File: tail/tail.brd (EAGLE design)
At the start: 63.2 x 30.5 mm, 6 parts

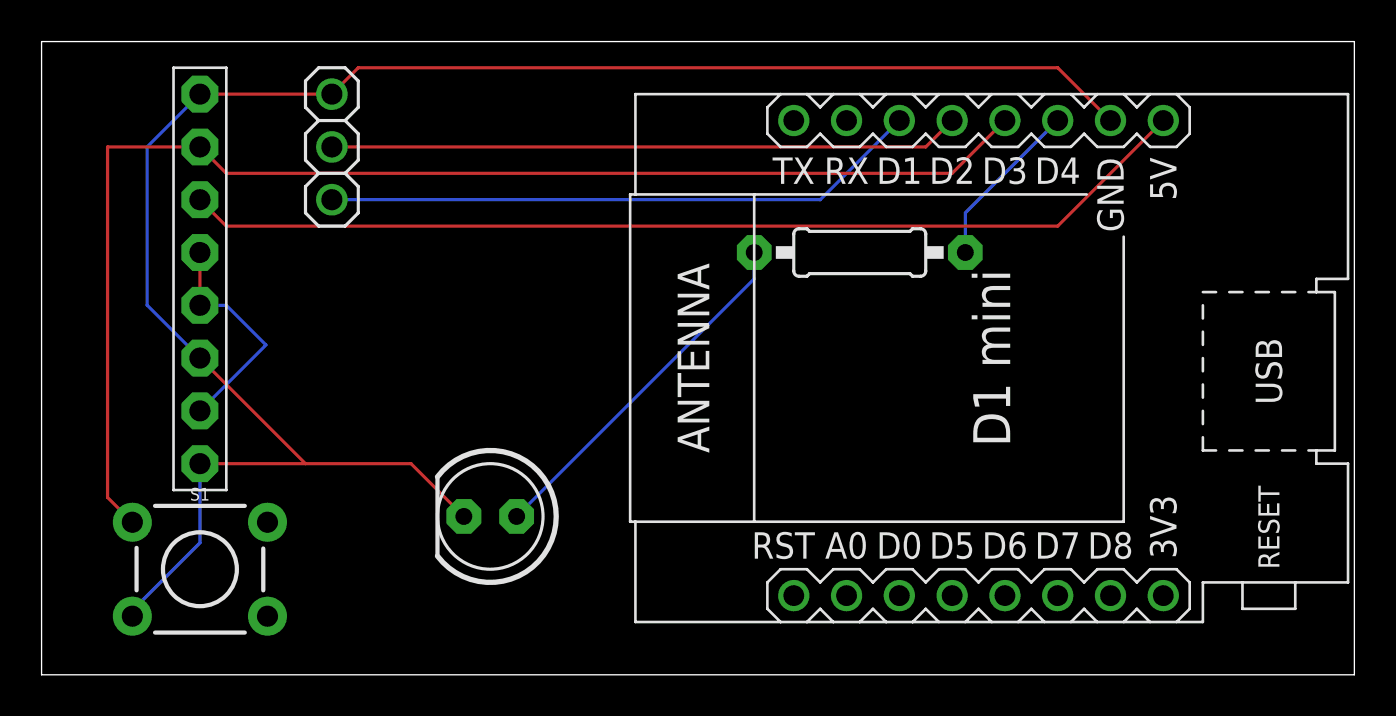
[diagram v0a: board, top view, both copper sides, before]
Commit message: Corrected spelling
On the PC, #include is not case sensitive. It is on Linux.
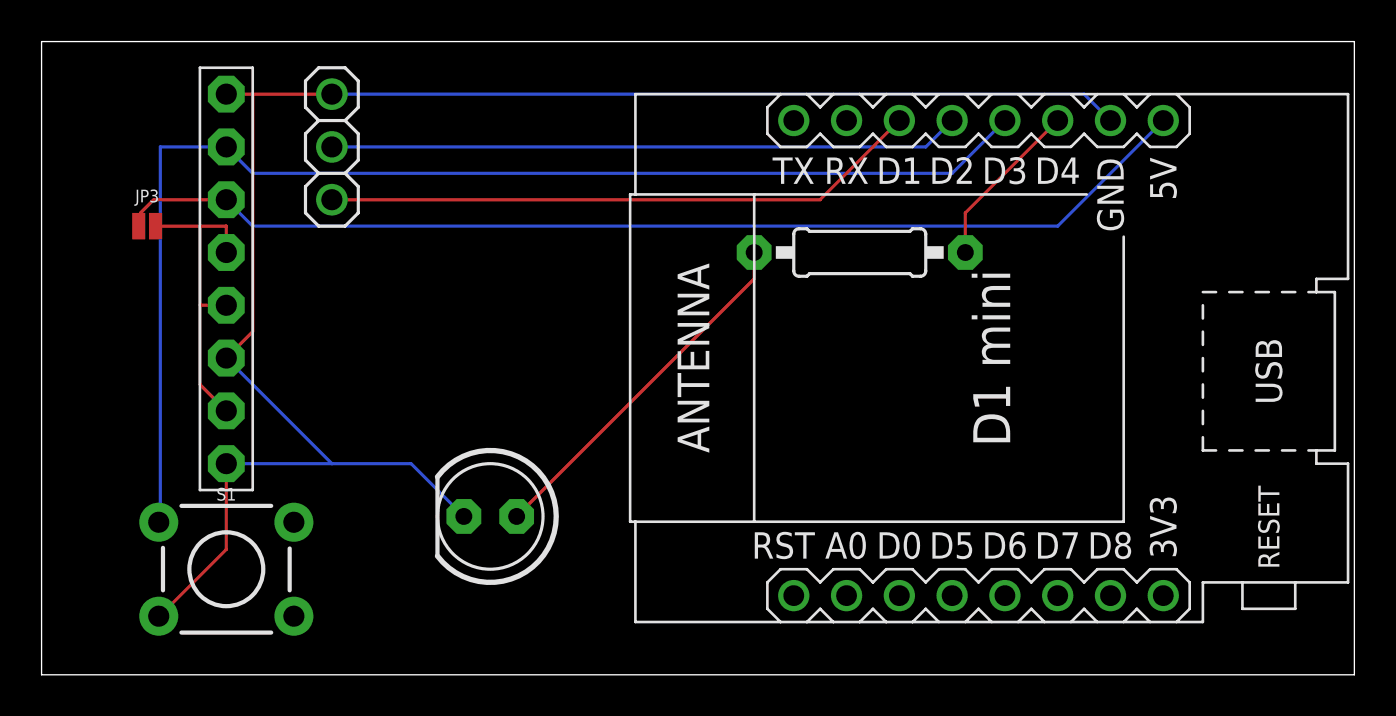
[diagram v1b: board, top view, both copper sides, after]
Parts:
- added JP3: (no value), SparkFun-Jumpers:SMT-JUMPER_2_NC_PASTE_NO-SILK
- moved JP1 1.27 mm to (8.89, 68.6)
- moved S1 1.27 mm to (8.89, 54.6)
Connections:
- net N$4: now also JP3.2
- net N$6: now also JP3.1
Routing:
- net 0: track 89.8 -> 84.7 mm
- net N$4: track 11.0 -> 15.4 mm
- net N$6: track 49.0 -> 52.8 mm
- net N$10: track 63.3 -> 60.3 mm
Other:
- board text added: "H-Bridge"
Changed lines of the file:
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@@
 <text x="2.794" y="77.597" size="1.27" layer="27" rot="R270">G +5  G +5    JMP  BTN</text>
 <text x="15.875" y="77.978" size="1.27" layer="27" rot="R270">D1 D2 G</text>
+<text x="18.415" y="77.978" size="1.27" layer="27" rot="R270">H-Bridge</text>
 </plain>
 <attributes>
@@
 <attribute name="VALUE" x="18.3896" y="58.9534" size="1.27" layer="27" ratio="10" rot="R180"/>
 </element>
-<element name="JP1" library="adafruit" package="1X08-BIG" value="" x="7.62" y="68.58" smashed="yes" rot="R90">
-<attribute name="VALUE" x="10.795" y="58.42" size="1.27" layer="27" rot="R90"/>
+<element name="JP1" library="adafruit" package="1X08-BIG" value="" x="8.89" y="68.58" smashed="yes" rot="R90">
+<attribute name="VALUE" x="12.065" y="58.42" size="1.27" layer="27" rot="R90"/>
 </element>
 <element name="R4" library="adafruit" library_urn="urn:adsk.eagle:library:420" package="0207/10" package3d_urn="urn:adsk.eagle:package:6240597/1" value="1K" x="39.37" y="69.85" smashed="yes">
@@
 <attribute name="VALUE" x="10.795" y="78.74" size="1.27" layer="27" rot="R270"/>
 </element>
-<element name="S1" library="SparkFun-Switches" library_urn="urn:adsk.eagle:library:535" package="TACTILE_SWITCH_PTH_6.0MM" package3d_urn="urn:adsk.eagle:package:40163/1" value="MOMENTARY-SWITCH-SPST-PTH-6.0MM" x="7.62" y="54.61" smashed="yes">
-<attribute name="NAME" x="7.62" y="57.912" size="0.6096" layer="25" font="vector" ratio="20" align="bottom-center"/>
-<attribute name="PROD_ID" value=" SWCH-08441" x="7.62" y="54.61" size="1.778" layer="27" display="off"/>
-<attribute name="SF_SKU" value="COM-00097" x="7.62" y="54.61" size="1.778" layer="27" display="off"/>
-<attribute name="VALUE" x="7.62" y="51.435" size="0.6096" layer="27" font="vector" ratio="20" align="top-center" display="off"/>
+<element name="S1" library="SparkFun-Switches" library_urn="urn:adsk.eagle:library:535" package="TACTILE_SWITCH_PTH_6.0MM" package3d_urn="urn:adsk.eagle:package:40163/1" value="MOMENTARY-SWITCH-SPST-PTH-6.0MM" x="8.89" y="54.61" smashed="yes">
+<attribute name="NAME" x="8.89" y="57.912" size="0.6096" layer="25" font="vector" ratio="20" align="bottom-center"/>
+<attribute name="PROD_ID" value=" SWCH-08441" x="8.89" y="54.61" size="1.778" layer="27" display="off"/>
+<attribute name="SF_SKU" value="COM-00097" x="8.89" y="54.61" size="1.778" layer="27" display="off"/>
+<attribute name="VALUE" x="8.89" y="51.435" size="0.6096" layer="27" font="vector" ratio="20" align="top-center" display="off"/>
+</element>
+<element name="JP3" library="SparkFun-Jumpers" library_urn="urn:adsk.eagle:library:528" package="SMT-JUMPER_2_NC_PASTE_NO-SILK" package3d_urn="urn:adsk.eagle:package:39283/1" value="" x="5.08" y="71.12" smashed="yes">
+<attribute name="NAME" x="5.08" y="72.263" size="0.6096" layer="25" font="vector" ratio="20" align="bottom-center"/>
+<attribute name="VALUE" x="5.08" y="69.977" size="0.6096" layer="27" font="vector" ratio="20" align="top-center"/>
 </element>
 </elements>
@@
 <contactref element="JP1" pad="8"/>
 <contactref element="S1" pad="3"/>
-<wire x1="17.78" y1="59.69" x2="20.32" y2="57.15" width="0.1524" layer="1"/>
-<wire x1="7.62" y1="59.69" x2="12.7" y2="59.69" width="0.1524" layer="1"/>
-<wire x1="12.7" y1="59.69" x2="17.78" y2="59.69" width="0.1524" layer="1"/>
-<wire x1="12.7" y1="59.69" x2="7.62" y2="64.77" width="0.1524" layer="1"/>
-<wire x1="7.62" y1="55.88" x2="4.445" y2="52.705" width="0.1524" layer="16"/>
-<wire x1="7.62" y1="59.69" x2="7.62" y2="55.88" width="0.1524" layer="16"/>
-<wire x1="4.445" y1="52.705" x2="4.3688" y2="52.3494" width="0.1524" layer="16"/>
-<wire x1="48.895" y1="78.74" x2="51.435" y2="76.2" width="0.1524" layer="1"/>
-<wire x1="48.895" y1="78.74" x2="15.24" y2="78.74" width="0.1524" layer="1"/>
-<wire x1="13.97" y1="77.47" x2="15.24" y2="78.74" width="0.1524" layer="1"/>
-<wire x1="13.97" y1="77.47" x2="7.62" y2="77.47" width="0.1524" layer="1"/>
-<wire x1="5.08" y1="67.31" x2="7.62" y2="64.77" width="0.1524" layer="16"/>
-<wire x1="5.08" y1="74.93" x2="5.08" y2="67.31" width="0.1524" layer="16"/>
-<wire x1="7.62" y1="77.47" x2="5.08" y2="74.93" width="0.1524" layer="16"/>
+<wire x1="17.78" y1="59.69" x2="20.32" y2="57.15" width="0.1524" layer="16"/>
+<wire x1="8.89" y1="59.69" x2="13.97" y2="59.69" width="0.1524" layer="16"/>
+<wire x1="13.97" y1="59.69" x2="17.78" y2="59.69" width="0.1524" layer="16"/>
+<wire x1="13.97" y1="59.69" x2="8.89" y2="64.77" width="0.1524" layer="16"/>
+<wire x1="8.89" y1="55.5625" x2="5.715" y2="52.3875" width="0.1524" layer="1"/>
+<wire x1="8.89" y1="59.69" x2="8.89" y2="55.5625" width="0.1524" layer="1"/>
+<wire x1="5.715" y1="52.3875" x2="5.6388" y2="52.3494" width="0.1524" layer="1"/>
+<wire x1="50.165" y1="77.47" x2="51.435" y2="76.2" width="0.1524" layer="16"/>
+<wire x1="13.97" y1="77.47" x2="50.165" y2="77.47" width="0.1524" layer="16"/>
+<wire x1="13.97" y1="77.47" x2="10.16" y2="77.47" width="0.1524" layer="1"/>
+<wire x1="10.16" y1="77.47" x2="8.89" y2="77.47" width="0.1524" layer="1"/>
+<wire x1="10.16" y1="66.04" x2="8.89" y2="64.77" width="0.1524" layer="1"/>
+<wire x1="10.16" y1="77.47" x2="10.16" y2="66.04" width="0.1524" layer="1"/>
 </signal>
 <signal name="N$8">
 <contactref element="R4" pad="2"/>
 <contactref element="W1" pad="JP2.6"/>
-<wire x1="44.45" y1="71.755" x2="48.895" y2="76.2" width="0.1524" layer="16"/>
-<wire x1="44.45" y1="69.85" x2="44.45" y2="71.755" width="0.1524" layer="16"/>
+<wire x1="44.45" y1="71.755" x2="48.895" y2="76.2" width="0.1524" layer="1"/>
+<wire x1="44.45" y1="69.85" x2="44.45" y2="71.755" width="0.1524" layer="1"/>
 </signal>
 <signal name="N$9">
 <contactref element="R4" pad="1"/>
 <contactref element="LED3" pad="A"/>
-<wire x1="34.29" y1="68.58" x2="22.86" y2="57.15" width="0.1524" layer="16"/>
-<wire x1="34.29" y1="69.85" x2="34.29" y2="68.58" width="0.1524" layer="16"/>
+<wire x1="34.29" y1="68.58" x2="22.86" y2="57.15" width="0.1524" layer="1"/>
+<wire x1="34.29" y1="69.85" x2="34.29" y2="68.58" width="0.1524" layer="1"/>
 </signal>
 <signal name="N$10">
@@
 <contactref element="JP1" pad="7"/>
 <contactref element="S1" pad="1"/>
-<wire x1="43.815" y1="73.66" x2="46.355" y2="76.2" width="0.1524" layer="1"/>
-<wire x1="8.89" y1="73.66" x2="43.815" y2="73.66" width="0.1524" layer="1"/>
-<wire x1="7.62" y1="74.93" x2="8.89" y2="73.66" width="0.1524" layer="1"/>
-<wire x1="3.175" y1="74.93" x2="3.175" y2="58.0644" width="0.1524" layer="1"/>
-<wire x1="4.3688" y1="56.8706" x2="3.175" y2="58.0644" width="0.1524" layer="1"/>
-<wire x1="7.62" y1="74.93" x2="3.175" y2="74.93" width="0.1524" layer="1"/>
+<wire x1="43.815" y1="73.66" x2="46.355" y2="76.2" width="0.1524" layer="16"/>
+<wire x1="10.16" y1="73.66" x2="43.815" y2="73.66" width="0.1524" layer="16"/>
+<wire x1="8.89" y1="74.93" x2="10.16" y2="73.66" width="0.1524" layer="16"/>
+<wire x1="5.715" y1="74.93" x2="5.715" y2="57.15" width="0.1524" layer="16"/>
+<wire x1="8.89" y1="74.93" x2="5.715" y2="74.93" width="0.1524" layer="16"/>
+<wire x1="5.715" y1="57.15" x2="5.6388" y2="56.8706" width="0.1524" layer="16"/>
 </signal>
 <signal name="N$2">
 <contactref element="W1" pad="JP2.4"/>
 <contactref element="JP2" pad="2"/>
-<wire x1="42.545" y1="74.93" x2="43.815" y2="76.2" width="0.1524" layer="1"/>
-<wire x1="13.97" y1="74.93" x2="42.545" y2="74.93" width="0.1524" layer="1"/>
+<wire x1="42.545" y1="74.93" x2="43.815" y2="76.2" width="0.1524" layer="16"/>
+<wire x1="13.97" y1="74.93" x2="42.545" y2="74.93" width="0.1524" layer="16"/>
 </signal>
 <signal name="N$3">
 <contactref element="W1" pad="JP2.3"/>
 <contactref element="JP2" pad="3"/>
-<wire x1="37.465" y1="72.39" x2="41.275" y2="76.2" width="0.1524" layer="16"/>
-<wire x1="13.97" y1="72.39" x2="37.465" y2="72.39" width="0.1524" layer="16"/>
+<wire x1="37.465" y1="72.39" x2="41.275" y2="76.2" width="0.1524" layer="1"/>
+<wire x1="13.97" y1="72.39" x2="37.465" y2="72.39" width="0.1524" layer="1"/>
 </signal>
 <signal name="N$4">
@@
 <contactref element="JP1" pad="4"/>
 <contactref element="JP1" pad="5"/>
-<wire x1="10.795" y1="65.405" x2="7.62" y2="62.23" width="0.1524" layer="16"/>
-<wire x1="10.795" y1="65.405" x2="8.89" y2="67.31" width="0.1524" layer="16"/>
-<wire x1="7.62" y1="67.31" x2="8.89" y2="67.31" width="0.1524" layer="16"/>
-<wire x1="7.62" y1="67.31" x2="7.62" y2="69.85" width="0.1524" layer="1"/>
+<contactref element="JP3" pad="2"/>
+<wire x1="8.89" y1="71.12" x2="7.62" y2="71.12" width="0.1524" layer="1"/>
+<wire x1="7.62" y1="71.12" x2="5.4864" y2="71.12" width="0.1524" layer="1"/>
+<wire x1="8.89" y1="69.85" x2="8.89" y2="71.12" width="0.1524" layer="1"/>
+<wire x1="7.62" y1="63.5" x2="8.89" y2="62.23" width="0.1524" layer="1"/>
+<wire x1="7.62" y1="71.12" x2="7.62" y2="67.31" width="0.1524" layer="1"/>
+<wire x1="7.62" y1="67.31" x2="7.62" y2="63.5" width="0.1524" layer="1"/>
+<wire x1="7.62" y1="67.31" x2="8.89" y2="67.31" width="0.1524" layer="1"/>
 </signal>
 <signal name="N$6">
 <contactref element="JP1" pad="6"/>
 <contactref element="W1" pad="JP2.8"/>
-<wire x1="48.895" y1="71.12" x2="53.975" y2="76.2" width="0.1524" layer="1"/>
-<wire x1="8.89" y1="71.12" x2="48.895" y2="71.12" width="0.1524" layer="1"/>
-<wire x1="7.62" y1="72.39" x2="8.89" y2="71.12" width="0.1524" layer="1"/>
+<contactref element="JP3" pad="1"/>
+<wire x1="4.7625" y1="71.755" x2="4.7625" y2="71.12" width="0.1524" layer="1"/>
+<wire x1="5.3975" y1="72.39" x2="4.7625" y2="71.755" width="0.1524" layer="1"/>
+<wire x1="8.89" y1="72.39" x2="5.3975" y2="72.39" width="0.1524" layer="1"/>
+<wire x1="4.7625" y1="71.12" x2="4.6736" y2="71.12" width="0.1524" layer="1"/>
+<wire x1="48.895" y1="71.12" x2="53.975" y2="76.2" width="0.1524" layer="16"/>
+<wire x1="10.16" y1="71.12" x2="48.895" y2="71.12" width="0.1524" layer="16"/>
+<wire x1="8.89" y1="72.39" x2="10.16" y2="71.12" width="0.1524" layer="16"/>
 </signal>
 </signals>
